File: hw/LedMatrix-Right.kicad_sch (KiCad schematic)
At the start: 87 parts, among them Q1400 DTA114E, Q1401 DTA114E, Q1402 DTA114E, Q1403 DTA114E, Q1404 DTA114E, Q1405 DTA114E, Q1406 DTA114E, Q1407 DTA114E, Q1408 DTA114E, Q1409 DTC114EE, Q1410 DTC114EE, Q1411 DTC114EE, Q1412 DTC114EE, Q1413 DTC114EE, Q1414 DTC114EE, Q1415 DTC114EE, Q1416 DTC114EE, Q1417 DTC114EE, Q1418 DTC114EE, Q1419 DTC114EE, Q1420 DTC114EE, Q1421 DTC114EE, Q1422 DTC114EE, Q1423 DTC114EE, X1400 Lightpipe-5x5mm-Dome, X1401 Lightpipe-5x5mm-Dome, X1402 Lightpipe-5x5mm-Dome

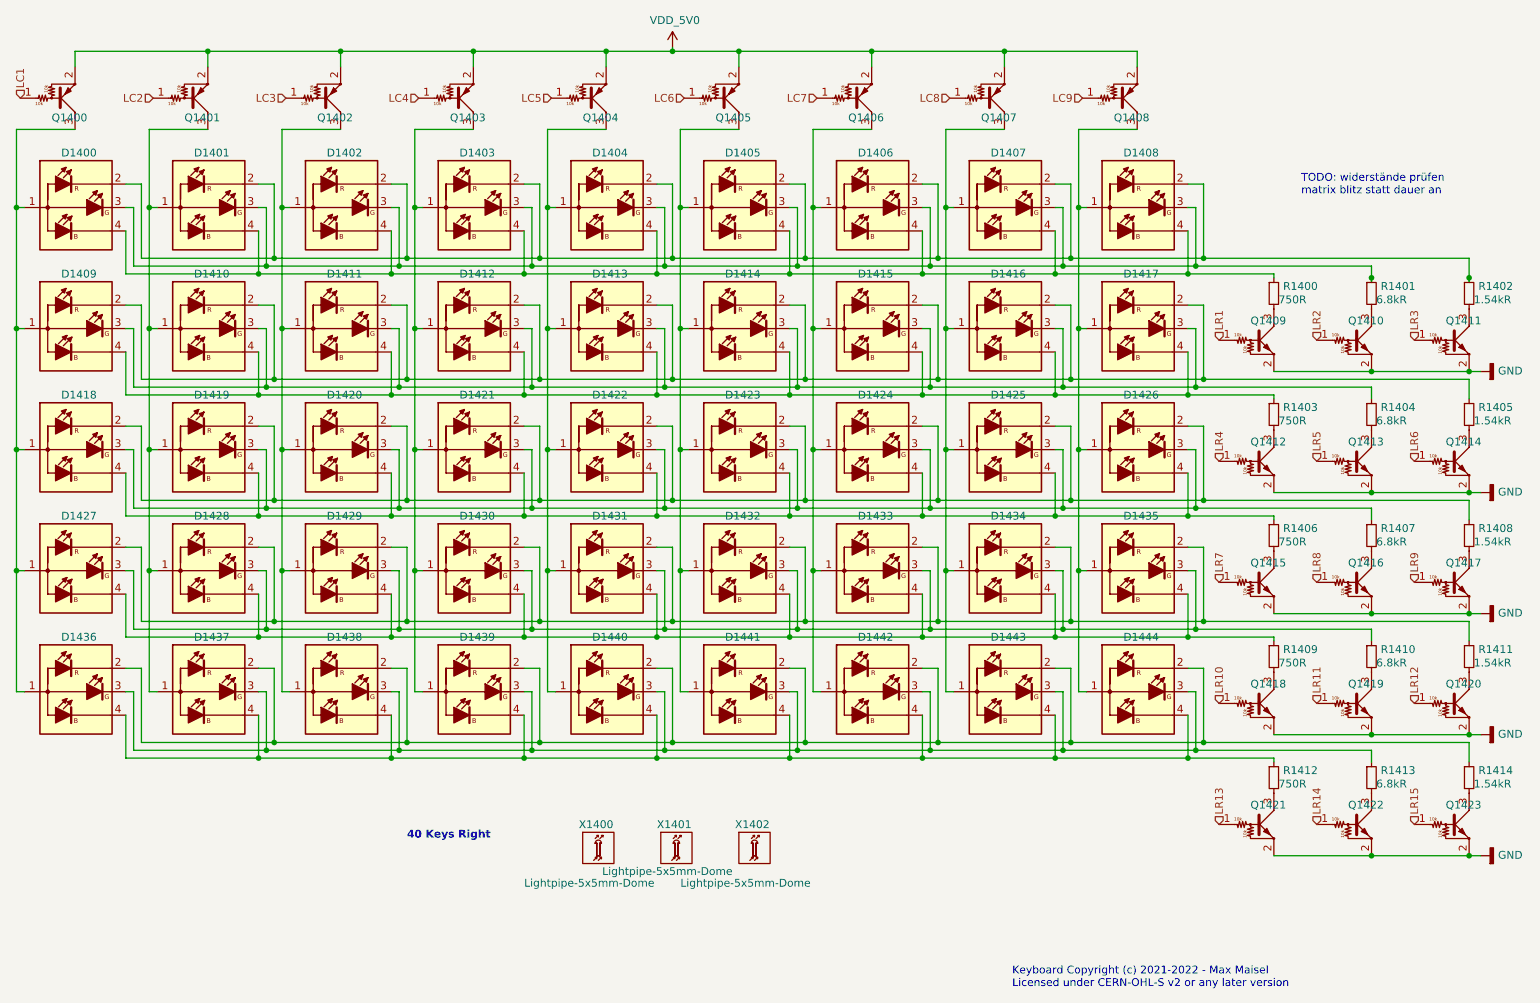
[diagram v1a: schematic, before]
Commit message: Update schematic:
- Add ESD protection.
- Adjust distance bolts so they fit to the MX mounting plate.
- Make key layout symmetric.
- Add resistor to TX driver outputs.
- Use alternate IO functions on inter-board connectors.
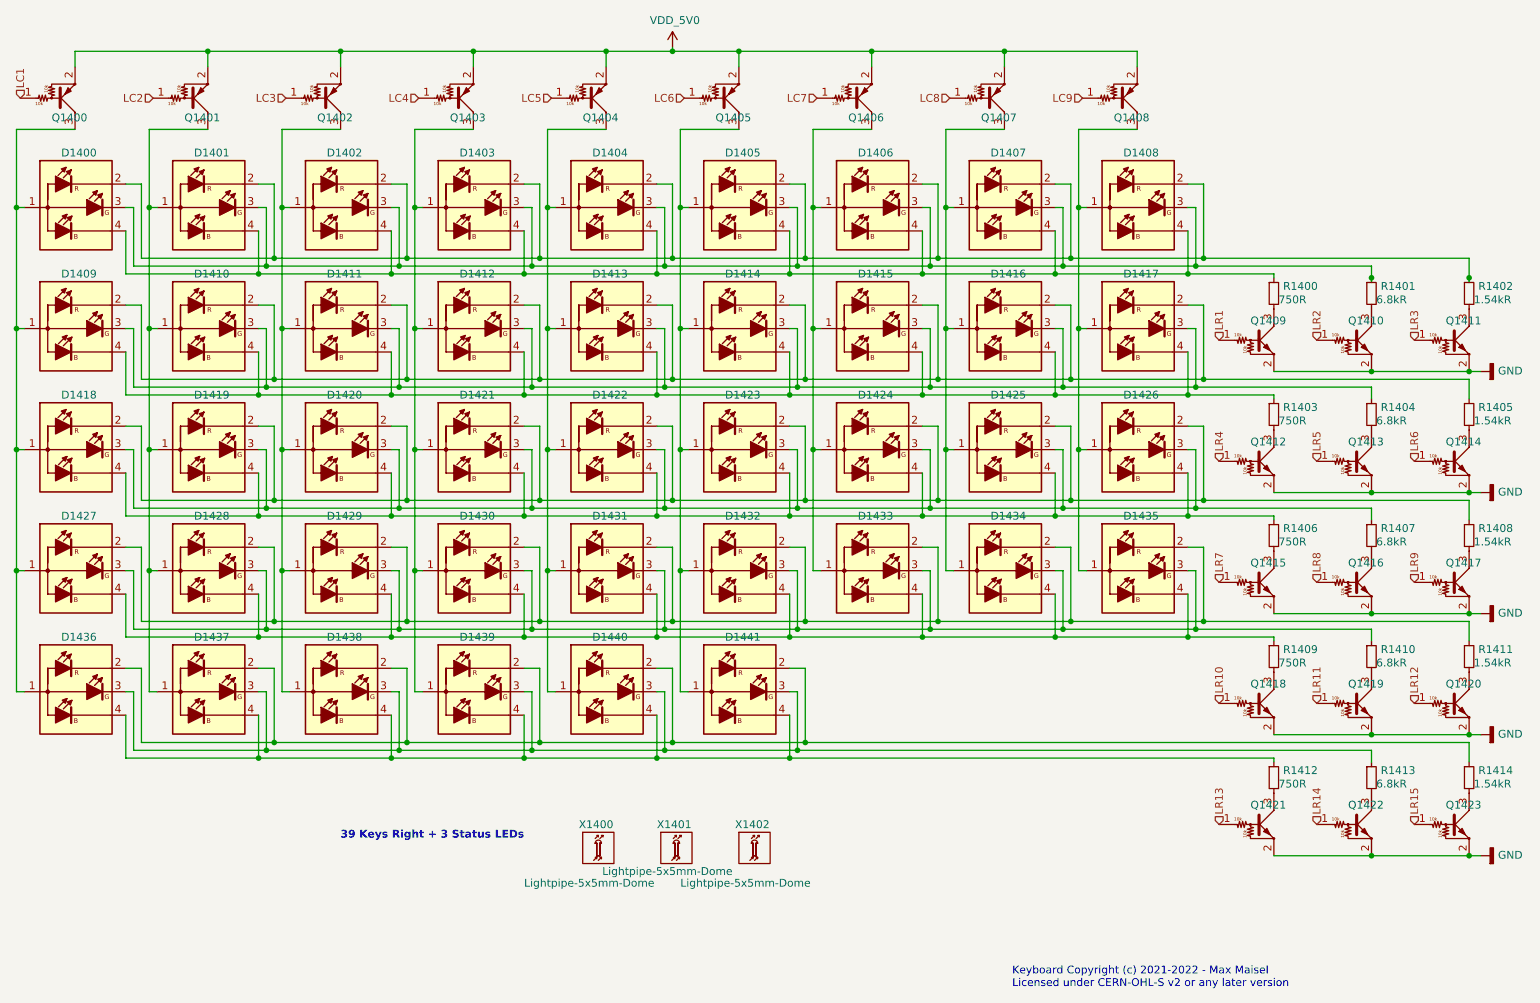
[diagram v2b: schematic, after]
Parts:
- removed D1442, D1443, D1444: APTF1616LSEEZGKQBKC, Keyboard:APTF1616-RGB, symbol Keyboard:APTF1616LSEEZGKQBKC
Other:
- note added: "39 Keys Right + 3 Status LEDs"
- note removed: "40 Keys Right"
- note removed: "TODO: widerstände prüfen matrix blitz statt dauer an"

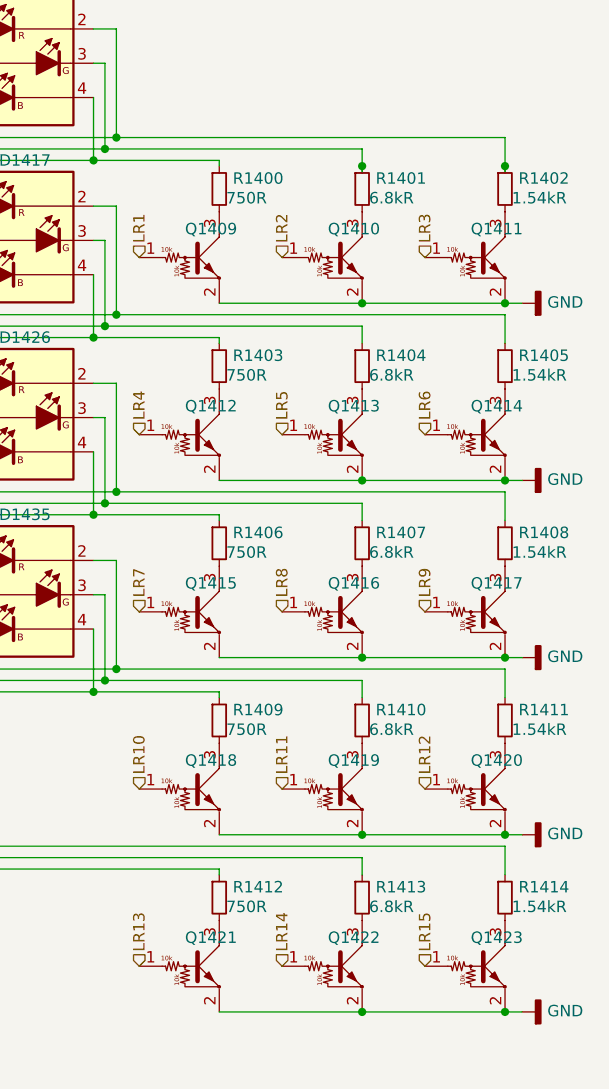
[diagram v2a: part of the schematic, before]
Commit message: Adjust LED matrix resistors.
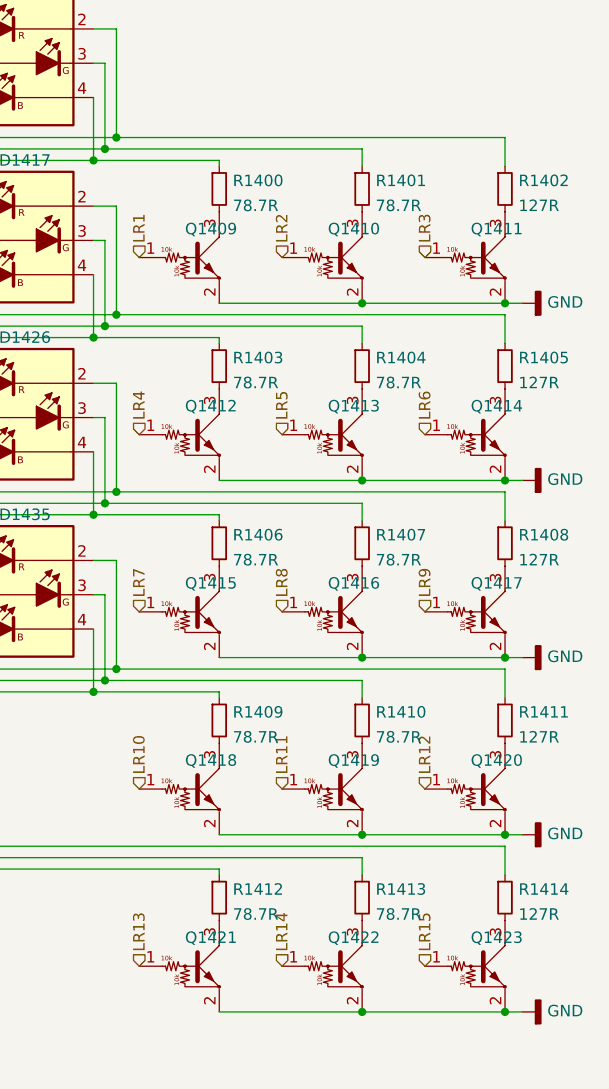
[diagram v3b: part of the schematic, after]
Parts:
- removed R1400, R1403, R1406, R1409, R1412: 750R, Keyboard:R_0402, symbol Keyboard:750R
- removed R1401, R1404, R1407, R1410, R1413: 6.8kR, Keyboard:R_0402, symbol Keyboard:6.8kR
- removed R1402, R1405, R1408, R1411, R1414: 1.54kR, Keyboard:R_0402, symbol Keyboard:1.54kR
- added R1400, R1401, R1403, R1404, R1406, R1407, R1409, R1410, R1412, R1413: 78.7R, Keyboard:R_0402, symbol Keyboard:78.7R
- added R1402, R1405, R1408, R1411, R1414: 127R, Keyboard:R_0402, symbol Keyboard:127R
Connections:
- net at D1436.2 (KR), D1437.2 (KR), D1438.2 (KR)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: now also R1414.1
- net at D1436.3 (KG), D1437.3 (KG), D1438.3 (KG)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: now also R1413.1
- net at D1436.4 (KB), D1437.4 (KB), D1438.4 (KB)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: now also R1412.1
- net at Q1423.3 (C): now also R1414.2
- net at Q1422.3 (C): now also R1413.2
- net at Q1421.3 (C): now also R1412.2
- net at D1400.2 (KR), D1401.2 (KR), D1402.2 (KR)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: now also R1402.1
- net at D1400.3 (KG), D1401.3 (KG), D1402.3 (KG)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: now also R1401.1
- net at D1400.4 (KB), D1401.4 (KB), D1402.4 (KB)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: now also R1400.1
- net at D1418.2 (KR), D1419.2 (KR), D1420.2 (KR)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: now also R1408.1
- net at D1418.3 (KG), D1419.3 (KG), D1420.3 (KG)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: now also R1407.1
- net at D1418.4 (KB), D1419.4 (KB), D1420.4 (KB)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: now also R1406.1
- net at D1427.2 (KR), D1428.2 (KR), D1429.2 (KR)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: now also R1411.1
- net at D1427.3 (KG), D1428.3 (KG), D1429.3 (KG)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: now also R1410.1
- net at D1427.4 (KB), D1428.4 (KB), D1429.4 (KB)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: now also R1409.1
- net at Q1409.3 (C): now also R1400.2
- net at Q1410.3 (C): now also R1401.2
- net at Q1411.3 (C): now also R1402.2
- net at D1409.2 (KR), D1410.2 (KR), D1411.2 (KR)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: now also R1405.1
- net at D1409.3 (KG), D1410.3 (KG), D1411.3 (KG)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: now also R1404.1
- net at D1409.4 (KB), D1410.4 (KB), D1411.4 (KB)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: now also R1403.1
- net at Q1417.3 (C): now also R1408.2
- net at Q1413.3 (C): now also R1404.2
- net at Q1414.3 (C): now also R1405.2
- net at Q1415.3 (C): now also R1406.2
- net at Q1418.3 (C): now also R1409.2
- net at Q1412.3 (C): now also R1403.2
- net at Q1420.3 (C): now also R1411.2
- net at Q1416.3 (C): now also R1407.2
- net at Q1419.3 (C): now also R1410.2
